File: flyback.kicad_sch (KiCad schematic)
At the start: 3 parts, among them U1 TPS23751PWP

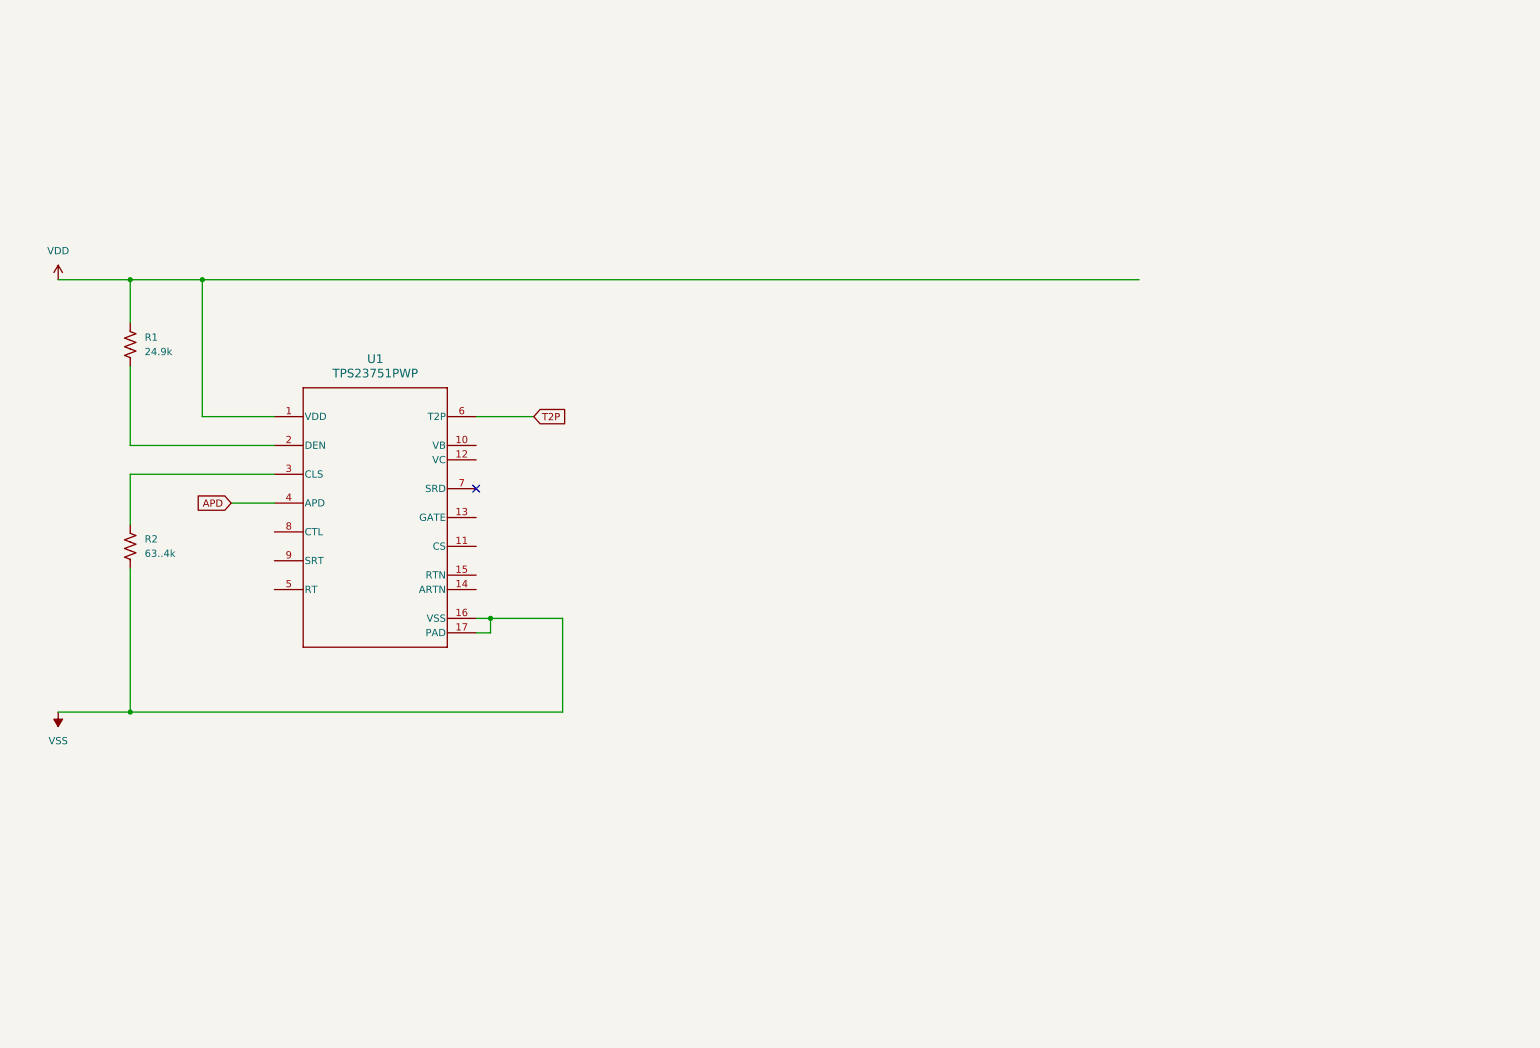
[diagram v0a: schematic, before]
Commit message: Working on flyback diode
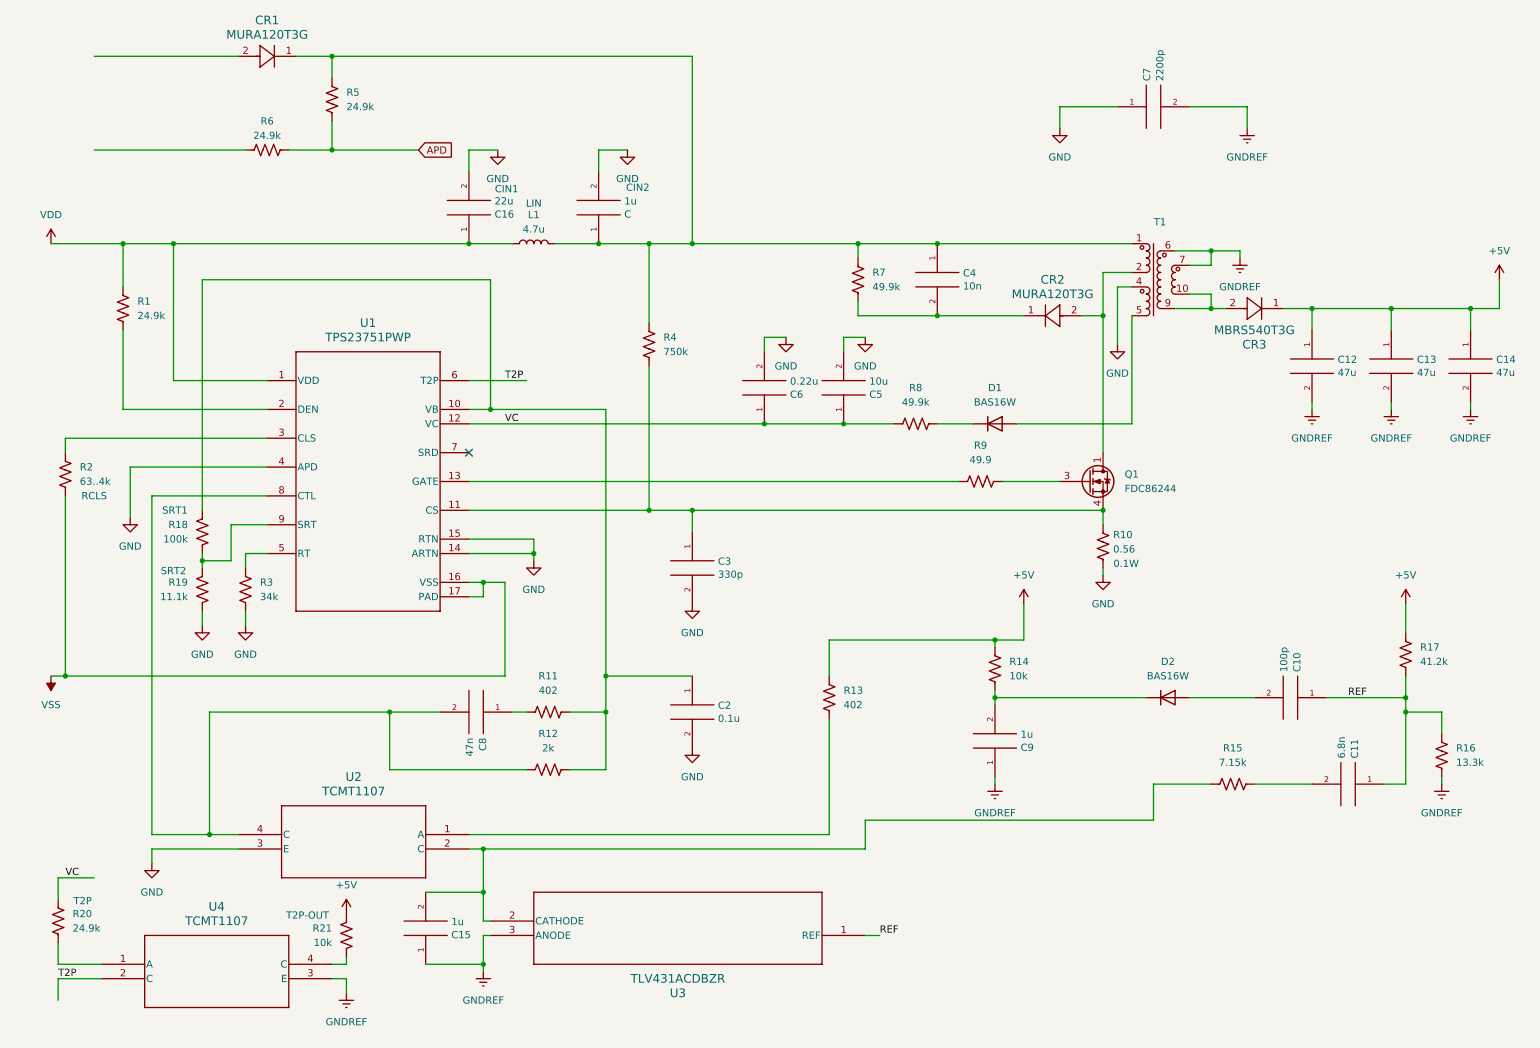
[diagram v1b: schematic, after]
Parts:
- added C, C15, C9: 1u, symbol PoE-rescue:C-pspice
- added C10: 100p, symbol PoE-rescue:C-pspice
- added C11: 6.8n, symbol PoE-rescue:C-pspice
- added C12, C13, C14: 47u, symbol PoE-rescue:C-pspice
- added C16: 22u, symbol PoE-rescue:C-pspice
- added C2: 0.1u, symbol PoE-rescue:C-pspice
- added C3: 330p, symbol PoE-rescue:C-pspice
- added C4: 10n, symbol PoE-rescue:C-pspice
- added C5: 10u, symbol PoE-rescue:C-pspice
- added C6: 0.22u, symbol PoE-rescue:C-pspice
- added C7: 2200p, symbol PoE-rescue:C-pspice
- added C8: 47n, symbol PoE-rescue:C-pspice
- added CR1, CR2: MURA120T3G, DIODE_TVS1SMAS5_4P57X2P92_ONS, symbol MURA120T3G:MURA120T3G
- added CR3: MBRS540T3G, DIODE_SMC_7P15X6P25_ONS, symbol MBRS540T3G:MBRS540T3G
- added D1, D2: BAS16W, Package_TO_SOT_SMD:SOT-323_SC-70, symbol Diode:BAS16W
- added L1: 4.7u, symbol Device:L
- added Q1: FDC86244, Package_TO_SOT_SMD:SuperSOT-6, symbol Transistor_FET:FDC86244
- added R10: 0.56, symbol Device:R_US
- added R11, R13: 402, 0402, symbol Device:R_US
- added R12: 2k, 0402, symbol Device:R_US
- added R14, R21: 10k, 0402, symbol Device:R_US
- added R15: 7.15k, 0402, symbol Device:R_US
- added R16: 13.3k, 0402, symbol Device:R_US
- added R17: 41.2k, 0402, symbol Device:R_US
- added R18: 100k, 0402, symbol Device:R_US
- added R19: 11.1k, 0402, symbol Device:R_US
- added R20, R5, R6: 24.9k, 0402, symbol Device:R_US
- added R3: 34k, 0402, symbol Device:R_US
- added R4: 750k, 0402, symbol Device:R_US
- added R7, R8: 49.9k, 0402, symbol Device:R_US
- added R9: 49.9, 0402, symbol Device:R_US
- added T1: ~, symbol 750311320:750311320
- added U2, U4: TCMT1107, SSOP4_4P40X2P85_VIS, symbol TCMT1107:TCMT1107
- added U3: TLV431ACDBZR, DBZ3, symbol TLV431ACDBZR:TLV431ACDBZR
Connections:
- net APD: now also R5.2, R6.1; no longer U1.4 (APD)
- net T2P: now also U4.2 (C)
- net VDD: now also C16.1, L1.1
- net at U1.10 (VB): now also C2.1, R11.1, R12.1, R18.1
- net at U1.11 (CS): now also C3.1, Q1.4 (S), R10.1, R4.2
- net VC: now reaches U1.12 (VC)
- net VC: now also C5.1, C6.1, R20.1, R8.2
- net at U1.13 (GATE): now also R9.2
- net GND: now reaches U1.14 (ARTN)
- net GND: now also U1.15 (RTN), U1.4 (APD), C.2, C16.2, C2.2, C3.2, C5.2, C6.2, C7.1, R10.2, R19.2, R3.2, T1.4, U2.3 (E)
- net at U1.5 (RT): now also R3.1
- net at U1.8 (CTL): now also C8.2, R12.2, U2.4 (C)
- net at U1.9 (SRT): now also R18.2, R19.1
- new net: CR3.2, T1.10, T1.9
- new net: Q1.3 (G), R9.1
- new net: C4.2, CR2.1, R7.2
- new net: CR2.2, Q1.1 (D), Q1.2 (D), Q1.5 (D), Q1.6 (D), T1.2
- new net: R13.2, U2.1 (A)
- new net: C15.2, R15.1, U2.2 (C), U3.2 (CATHODE)
- new net: C10.2, D2.1 (A)
- new net: C9.2, D2.3 (K), R14.2
- new net: C11.2, R15.2
- new net: C.1, C4.1, CR1.1, L1.2, R4.1, R5.1, R7.1, T1.1
- new net: C8.1, R11.2
- new net: D1.1 (A), T1.5
- new net: R20.2, U4.1 (A)
- new net: R21.2, U4.4 (C)
- new net: D1.3 (K), R8.1
- new net +5V: C12.1, C13.1, C14.1, CR3.1, R13.1, R14.1, R17.1, R21.1
- new net GNDREF: C12.2, C13.2, C14.2, C15.1, C7.2, C9.1, R16.2, T1.6, T1.7, U3.3 (ANODE), U4.3 (E)
- new net REF: C10.1, C11.1, R16.1, R17.2, U3.1 (REF)
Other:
- moved on the sheet: R1, R2, U1

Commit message: Added basic SPICE sim
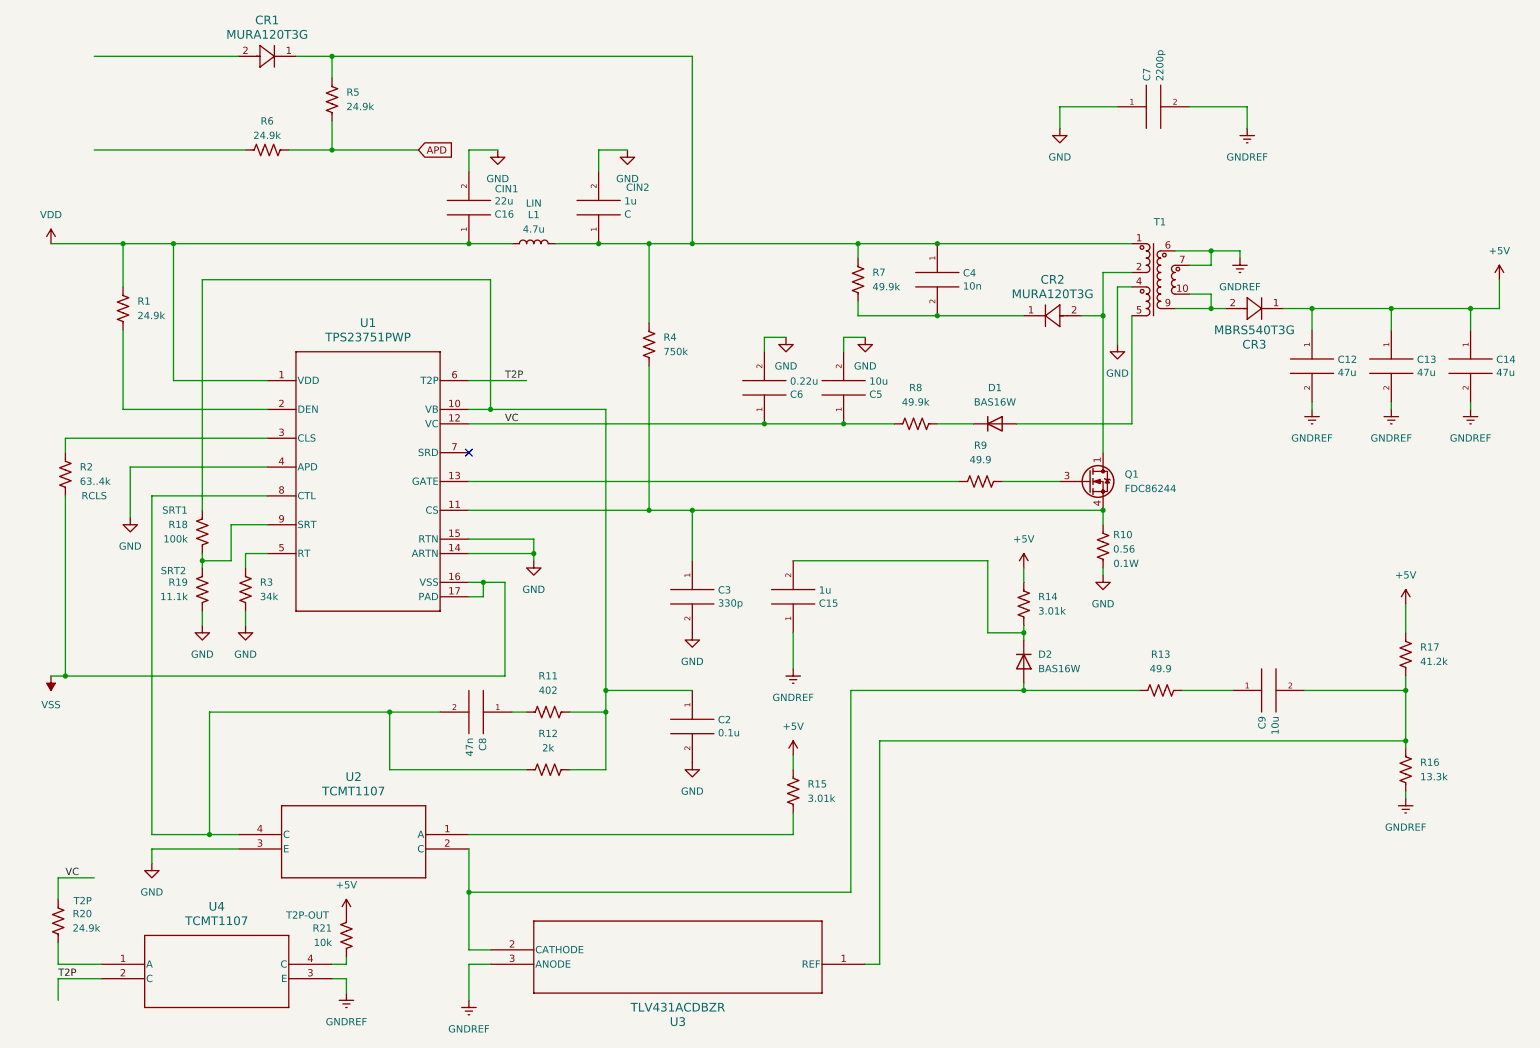
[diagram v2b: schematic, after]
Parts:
- removed C10: 100p, symbol PoE-rescue:C-pspice
- removed C11: 6.8n, symbol PoE-rescue:C-pspice
- C9: value 1u -> 10u
- R13: value 402 -> 49.9
- R14: value 10k -> 3.01k
- R15: value 7.15k -> 3.01k
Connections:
- net +5V: now also R14.2, R15.2; no longer R13.1, R14.1
- net GNDREF: no longer C9.1
- net at U2.1 (A): now also R15.1; no longer R13.2
- net at U2.2 (C), U3.2 (CATHODE): now also D2.1 (A), R13.2; no longer C15.2, R15.1
- net REF: no longer names the net of R16.1, R17.2, U3.1 (REF)
- net REF: now also C9.2
- new net: C9.1, R13.1
- new net: C15.2, D2.3 (K), R14.1
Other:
- moved on the sheet: C15, C2, C3, R16, U3

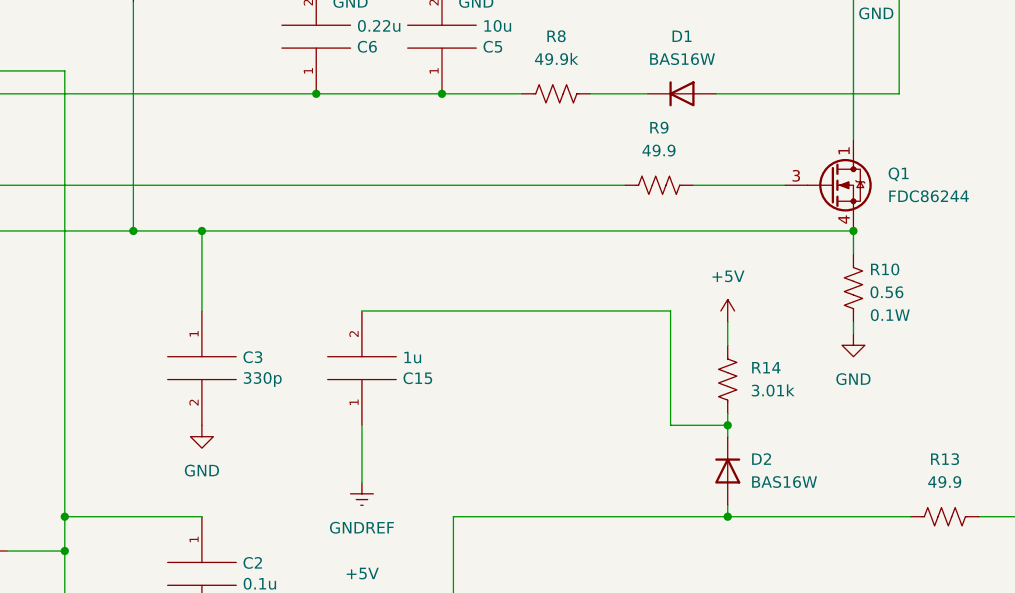
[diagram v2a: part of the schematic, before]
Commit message: More updates, added bus
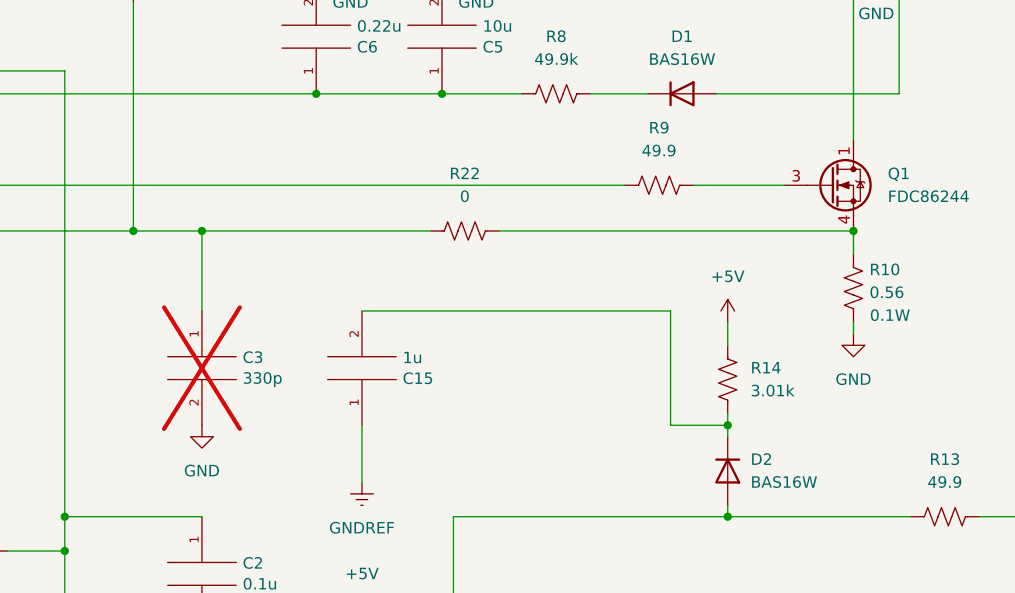
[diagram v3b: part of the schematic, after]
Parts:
- added R22: 0, 0402, symbol Device:R_US
- C3: now not fitted
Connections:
- net at C3.1, R4.2, U1.11 (CS): now also R22.2; no longer Q1.4 (S), R10.1
- new net: Q1.4 (S), R10.1, R22.1
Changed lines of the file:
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@@
 	(wire
 		(pts
-			(xy 137.16 104.14) (xy 209.55 104.14)
+			(xy 137.16 104.14) (xy 162.56 104.14)
 		)
 		(stroke
@@
 	(wire
 		(pts
+			(xy 170.18 104.14) (xy 209.55 104.14)
+		)
+		(stroke
+			(width 0)
+			(type default)
+		)
+	)
+	(wire
+		(pts
 			(xy 274.32 85.09) (xy 274.32 86.36)
 		)
@@
 		(in_bom yes)
 		(on_board yes)
-		(dnp no)
+		(dnp yes)
 		(property "Reference" "C3"
 			(at 141.6812 118.2116 0)
@@
 					(unit 1)
 				)
+			)
+		)
+	)
+	(symbol
+		(lib_id "Device:R_US")
+		(at 166.37 104.14 270)
+		(unit 1)
+		(exclude_from_sim no)
+		(in_bom yes)
+		(on_board yes)
+		(dnp no)
+		(fields_autoplaced yes)
+		(property "Reference" "R22"
+			(at 166.37 97.79 90)
+			(effects
+				(font
+					(size 1.27 1.27)
+				)
+			)
+		)
+		(property "Value" "0"
+			(at 166.37 100.33 90)
+			(effects
+				(font
+					(size 1.27 1.27)
+				)
+			)
+		)
+		(property "Footprint" "0402"
+			(at 166.116 105.156 90)
+			(effects
+				(font
+					(size 1.27 1.27)
+				)
+				(hide yes)
+			)
+		)
+		(property "Datasheet" "~"
+			(at 166.37 104.14 0)
+			(effects
+				(font
+					(size 1.27 1.27)
+				)
+				(hide yes)
+			)
+		)
+		(property "Description" "Resistor, US symbol"
+			(at 166.37 104.14 0)
+			(effects
+				(font
+					(size 1.27 1.27)
+				)
+				(hide yes)
+			)
+		)
+		(pin "1"
+		)
+		(pin "2"
+		)
+		(instances
+			(project "PoE"
+				(path "/e8d70991-5081-4afb-b8c3-5ce9f62355e0/1fdbb5e2-ecd4-47ea-a63c-f2f18c06d291"
+					(reference "R22")
+					(unit 1)
+				)

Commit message: Minor updates and adding footprints
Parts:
- C201: renamed from C7; footprint (none) -> SparkFun-Capacitor:C_0402_1005Metric
- C204: renamed from C4; footprint (none) -> SparkFun-Capacitor:C_0402_1005Metric
- C208: renamed from C6; footprint (none) -> SparkFun-Capacitor:C_0402_1005Metric
- C210: renamed from C3; footprint (none) -> SparkFun-Capacitor:C_0402_1005Metric
- C213: renamed from C8; footprint (none) -> SparkFun-Capacitor:C_0402_1005Metric
- C214: renamed from C2; footprint (none) -> SparkFun-Capacitor:C_0402_1005Metric
- CR201: renamed from CR1; footprint DIODE_TVS1SMAS5_4P57X2P92_ONS -> footprints:DIODE_TVS1SMAS5_4P57X2P92_ONS
- CR202: renamed from CR3; footprint DIODE_SMC_7P15X6P25_ONS -> footprints:DIODE_SMC_7P15X6P25_ONS
- CR203: renamed from CR2; footprint DIODE_TVS1SMAS5_4P57X2P92_ONS -> footprints:DIODE_TVS1SMAS5_4P57X2P92_ONS
- R201: renamed from R5; footprint 0402 -> SparkFun-Capacitor:C_0402_1005Metric
- R202: renamed from R6; footprint 0402 -> Resistor_SMD:R_01005_0402Metric
- R203: renamed from R7; footprint 0402 -> Resistor_SMD:R_0402_1005Metric
- R204: renamed from R1; footprint 0402 -> Resistor_SMD:R_01005_0402Metric
- R205: renamed from R4; footprint 0402 -> Resistor_SMD:R_01005_0402Metric
- R206: renamed from R8; footprint 0402 -> Resistor_SMD:R_01005_0402Metric
- R207: renamed from R2; footprint 0402 -> Resistor_SMD:R_01005_0402Metric
- R208: renamed from R9; footprint 0402 -> Resistor_SMD:R_01005_0402Metric
- R209: renamed from R22; footprint 0402 -> Resistor_SMD:R_01005_0402Metric
- R210: renamed from R18; footprint 0402 -> Resistor_SMD:R_01005_0402Metric
- R212: renamed from R19; footprint 0402 -> Resistor_SMD:R_0402_1005Metric
- R213: renamed from R3; footprint 0402 -> Resistor_SMD:R_0402_1005Metric
- R214: renamed from R14; footprint 0402 -> Resistor_SMD:R_0402_1005Metric
- R215: renamed from R17; footprint 0402 -> Resistor_SMD:R_0402_1005Metric
- R216: renamed from R13; footprint 0402 -> Resistor_SMD:R_0402_1005Metric
- R217: renamed from R11; footprint 0402 -> Resistor_SMD:R_0402_1005Metric
- R218: renamed from R12; footprint 0402 -> Resistor_SMD:R_0402_1005Metric
- R219: renamed from R16; footprint 0402 -> Resistor_SMD:R_0402_1005Metric
- R220: renamed from R15; footprint 0402 -> Resistor_SMD:R_0402_1005Metric
- R221: renamed from R20; footprint 0402 -> Resistor_SMD:R_0402_1005Metric
- R222: renamed from R21; footprint 0402 -> Resistor_SMD:R_0402_1005Metric
- U201: renamed from U1; footprint PWP0016J_N -> footprints:PWP0016J_N
- U202: renamed from U2; footprint SSOP4_4P40X2P85_VIS -> footprints:SSOP4_4P40X2P85_VIS
- U203: renamed from U4; footprint SSOP4_4P40X2P85_VIS -> footprints:SSOP4_4P40X2P85_VIS
- U204: renamed from U3; footprint DBZ3 -> footprints:DBZ3
- renumbered C16 to C202, C to C203, C12 to C205, C13 to C206, C14 to C207, C5 to C209, C15 to C211, C9 to C212, D1 to D201, D2 to D202, L1 to L201, Q1 to Q201, R10 to R211, T1 to T201

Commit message: Found footprints
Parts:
- removed R221: 24.9k, Resistor_SMD:R_0402_1005Metric, symbol Device:R_US
- removed R222: 10k, Resistor_SMD:R_0402_1005Metric, symbol Device:R_US
- removed U203: TCMT1107, footprints:SSOP4_4P40X2P85_VIS, symbol TCMT1107:TCMT1107
- added TP2001, TP2002: TestPoint, SparkFun-Connector:TestPoint-1.0mm, symbol Connector:TestPoint
- C2002: renamed from C202; footprint (none) -> footprints:CAP_WCAP-ASLI_06p3X05p5_WRE
- C2003: renamed from C203; footprint (none) -> footprints:CAP_WCAP-ASLI_06p3X05p5_WRE
- C2005: renamed from C205; footprint (none) -> footprints:CAP_WCAP-ASLI_06p3X05p5_WRE
- C2006: renamed from C206; footprint (none) -> footprints:CAP_WCAP-ASLI_06p3X05p5_WRE
- C2007: renamed from C207; footprint (none) -> footprints:CAP_WCAP-ASLI_06p3X05p5_WRE
- C2009: renamed from C209; footprint (none) -> footprints:CAP_WCAP-ASLI_06p3X05p5_WRE
- C2011: renamed from C211; footprint (none) -> Capacitor_SMD:C_0402_1005Metric
- C2012: renamed from C212; footprint (none) -> Capacitor_SMD:C_0603_1608Metric
- L2001: renamed from L201; footprint (none) -> Inductor_SMD:L_Abracon_ASPI-4030S
- R2001: renamed from R201; footprint SparkFun-Capacitor:C_0402_1005Metric -> Resistor_SMD:R_0402_1005Metric
- R2006: renamed from R206; value 49.9k -> 49.9
- R2011: renamed from R211; footprint (none) -> Resistor_SMD:R_0603_1608Metric
- T2001: renamed from T201; footprint (none) -> footprints:750311320
- renumbered C201 to C2001, C204 to C2004, C208 to C2008, C210 to C2010, C213 to C2013, C214 to C2014, CR201 to CR2001, CR202 to CR2002, CR203 to CR2003, D201 to D2001, D202 to D2002, Q201 to Q2001, R202 to R2002, R203 to R2003, R204 to R2004, R205 to R2005, R207 to R2007, R208 to R2008, R209 to R2009, R210 to R2010, R212 to R2012, R213 to R2013, R214 to R2014, R215 to R2015, R216 to R2016, R217 to R2017, R218 to R2018, R219 to R2019, R220 to R2020, U201 to U2001, U202 to U2002, U204 to U2003
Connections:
- net at CR2001.2: now also TP2001.1
- net at R2002.2: now also TP2002.1
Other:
- moved on the sheet: C2005, C2006, C2007
